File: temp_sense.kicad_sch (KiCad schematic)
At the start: 0 parts

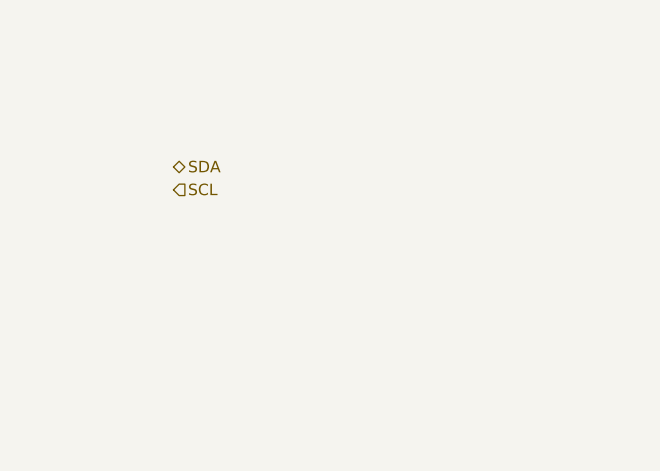
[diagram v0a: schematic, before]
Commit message: Added USB to UART circuitry, cleaned up top sheets, added more supporting circuitry for TX MCU
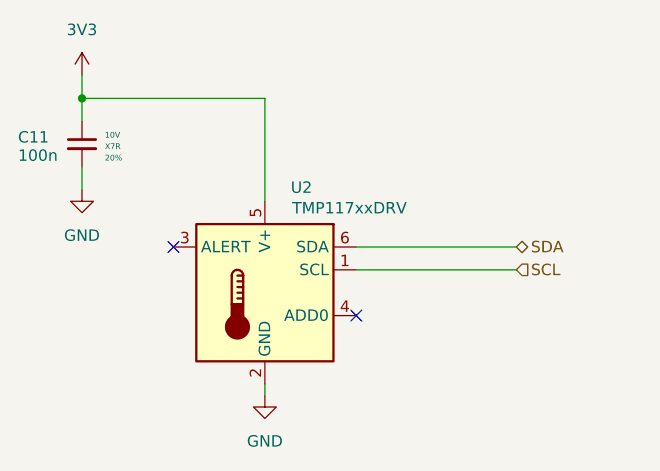
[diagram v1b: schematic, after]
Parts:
- added C11: 100n, Capacitor_SMD:C_0603_1608Metric_Pad1.08x0.95mm_HandSolder, symbol AERO_Capacitors:C_0603
- added U2: TMP117xxDRV, Package_SON:WSON-6-1EP_2x2mm_P0.65mm_EP1x1.6mm, symbol Sensor_Temperature:TMP117xxDRV
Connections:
- net SCL: now also U2.1 (SCL)
- net SDA: now also U2.6 (SDA)
- new net 3V3: C11.1, U2.5 (V+)
- new net GND: C11.2, U2.2 (GND)
- no-connect marks 0 -> 2

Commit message: Finished schematic, added power section for external power (both power supply and battery), added current sensing for TX microcontroller
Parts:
- renumbered C11 to C16, U2 to U3
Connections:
- net 3V3 renamed TX3V3
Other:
- note added: "From Datasheet:"
